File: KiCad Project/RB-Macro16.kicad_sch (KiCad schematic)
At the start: 67 parts, among them J1 USB_C_Receptacle, J2 AVR-ISP-6, K0A1 KEYSW, K0B1 KEYSW, K0C1 KEYSW, K0D1 KEYSW, K1A1 KEYSW, K1B1 KEYSW, K1C1 KEYSW, K1D1 KEYSW, K2A1 KEYSW, K2B1 KEYSW, K2C1 KEYSW, K2D1 KEYSW, K3A1 KEYSW, K3B1 KEYSW, K3C1 KEYSW, K3D1 KEYSW, SW1 SW_PUSH, U1 ATMEGA32U4, U2 CherryMX_LTST-A683CEGBW, X1 XTAL_GND

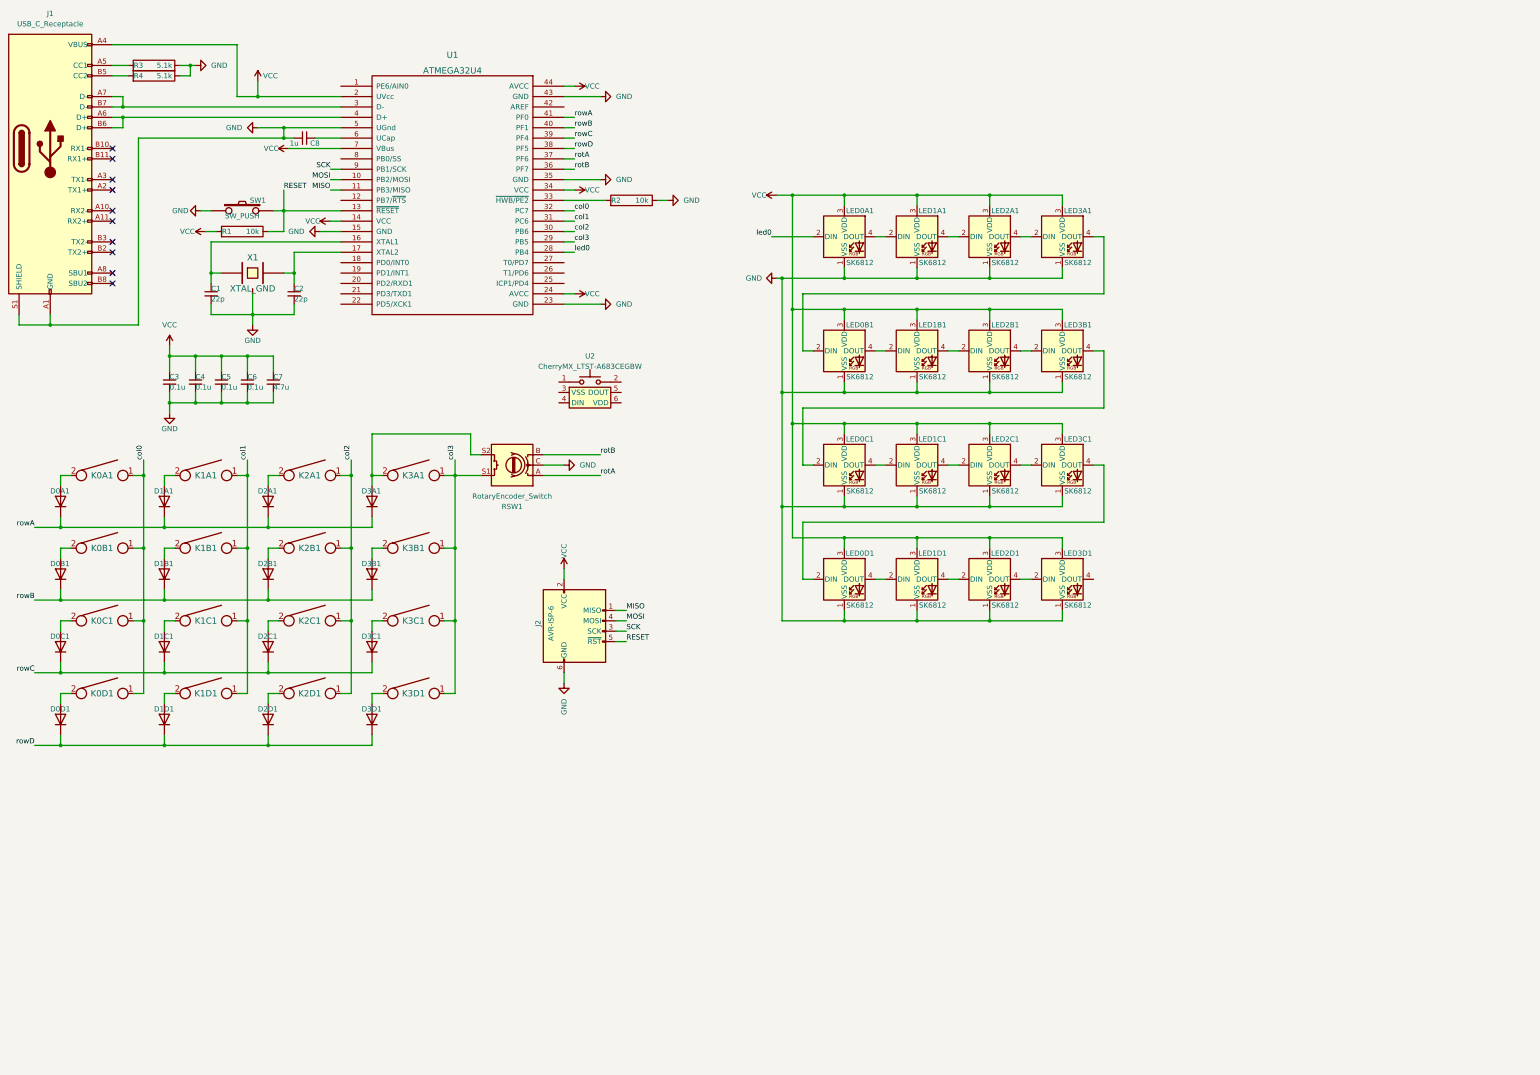
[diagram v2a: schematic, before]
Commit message: Abandoned New Swtich
Can't find LED new switch footprint uses. Began working on footprint for SK6812MINI-E from Adafruit as a replacement. Added capacitors to LED array and rebuilt it.
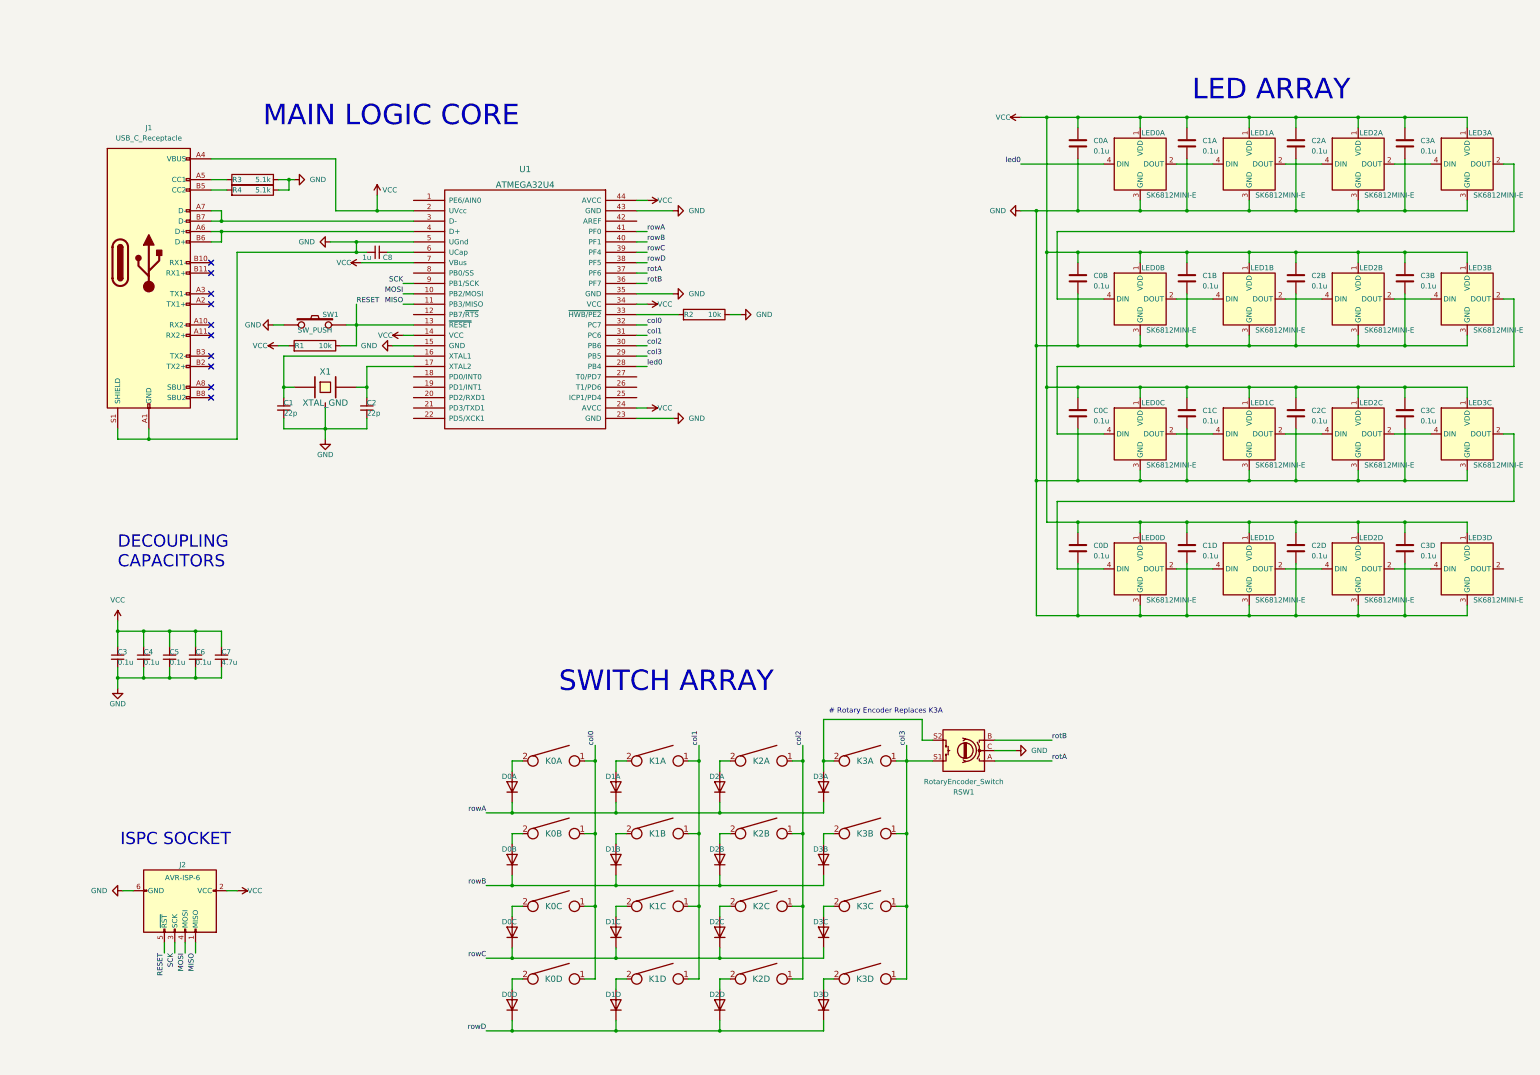
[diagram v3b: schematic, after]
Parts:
- removed LED0A1, LED0B1, LED0C1, LED0D1, LED1A1, LED1B1, LED1C1, LED1D1, LED2A1, LED2B1, LED2C1, LED2D1, LED3A1, LED3B1, LED3C1, LED3D1: SK6812, LED_SMD:LED_SK6812_EC15_1.5x1.5mm, symbol LED:SK6812
- removed U2: CherryMX_LTST-A683CEGBW, CherryMX_KailhSocket_LTST-A683CEGBW:CherryMX_1.00u_KailhSocket_LTST-A683CEGBW, symbol CherryMX:CherryMX_LTST-A683CEGBW
- added C0A, C0B, C0C, C0D, C1A, C1B, C1C, C1D, C2A, C2B, C2C, C2D, C3A, C3B, C3C, C3D: 0.1u, symbol Device:C
- added LED0A, LED0B, LED0C, LED0D, LED1A, LED1B, LED1C, LED1D, LED2A, LED2B, LED2C, LED2D, LED3A, LED3B, LED3C, LED3D: SK6812MINI-E, symbol RB_KeyboardParts:SK6812MINI-E
- J2: footprint keyboard_parts:AVR_ICSP_3x2 -> keyboard_parts.pretty-master:AVR_ICSP_3x2
- K0A: renamed from K0A1; footprint CherryMX_KailhSocket_LED:CherryMX_1.00u_KailhSocket_LED -> keyswitches.pretty-master:Kailh_socket_MX
- K0B: renamed from K0B1; footprint CherryMX_KailhSocket_LED:CherryMX_1.00u_KailhSocket_LED -> keyswitches.pretty-master:Kailh_socket_MX
- K0C: renamed from K0C1; footprint CherryMX_KailhSocket_LED:CherryMX_1.00u_KailhSocket_LED -> keyswitches.pretty-master:Kailh_socket_MX
- K0D: renamed from K0D1; footprint CherryMX_KailhSocket_LED:CherryMX_1.00u_KailhSocket_LED -> keyswitches.pretty-master:Kailh_socket_MX
- K1A: renamed from K1A1; footprint CherryMX_KailhSocket_LED:CherryMX_1.00u_KailhSocket_LED -> keyswitches.pretty-master:Kailh_socket_MX
- K1B: renamed from K1B1; footprint CherryMX_KailhSocket_LED:CherryMX_1.00u_KailhSocket_LED -> keyswitches.pretty-master:Kailh_socket_MX
- K1C: renamed from K1C1; footprint CherryMX_KailhSocket_LED:CherryMX_1.00u_KailhSocket_LED -> keyswitches.pretty-master:Kailh_socket_MX
- K1D: renamed from K1D1; footprint CherryMX_KailhSocket_LED:CherryMX_1.00u_KailhSocket_LED -> keyswitches.pretty-master:Kailh_socket_MX
- K2A: renamed from K2A1; footprint CherryMX_KailhSocket_LED:CherryMX_1.00u_KailhSocket_LED -> keyswitches.pretty-master:Kailh_socket_MX
- K2B: renamed from K2B1; footprint CherryMX_KailhSocket_LED:CherryMX_1.00u_KailhSocket_LED -> keyswitches.pretty-master:Kailh_socket_MX
- K2C: renamed from K2C1; footprint CherryMX_KailhSocket_LED:CherryMX_1.00u_KailhSocket_LED -> keyswitches.pretty-master:Kailh_socket_MX
- K2D: renamed from K2D1; footprint CherryMX_KailhSocket_LED:CherryMX_1.00u_KailhSocket_LED -> keyswitches.pretty-master:Kailh_socket_MX
- K3A: renamed from K3A1; footprint CherryMX_KailhSocket_LED:CherryMX_1.00u_KailhSocket_LED -> keyswitches.pretty-master:Kailh_socket_MX
- K3B: renamed from K3B1; footprint CherryMX_KailhSocket_LED:CherryMX_1.00u_KailhSocket_LED -> keyswitches.pretty-master:Kailh_socket_MX
- K3C: renamed from K3C1; footprint CherryMX_KailhSocket_LED:CherryMX_1.00u_KailhSocket_LED -> keyswitches.pretty-master:Kailh_socket_MX
- K3D: renamed from K3D1; footprint CherryMX_KailhSocket_LED:CherryMX_1.00u_KailhSocket_LED -> keyswitches.pretty-master:Kailh_socket_MX
- renumbered D0A1 to D0A, D0B1 to D0B, D0C1 to D0C, D0D1 to D0D, D1A1 to D1A, D1B1 to D1B, D1C1 to D1C, D1D1 to D1D, D2A1 to D2A, D2B1 to D2B, D2C1 to D2C, D2D1 to D2D, D3A1 to D3A, D3B1 to D3B, D3C1 to D3C, D3D1 to D3D
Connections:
- net GND: now also C0A.2, C0B.2, C0C.2, C0D.2, C1A.2, C1B.2, C1C.2, C1D.2, C2A.2, C2B.2, C2C.2, C2D.2, C3A.2, C3B.2, C3C.2, C3D.2, LED0A.3 (GND), LED0B.3 (GND), LED0C.3 (GND), LED0D.3 (GND), LED1A.3 (GND), LED1B.3 (GND), LED1C.3 (GND), LED1D.3 (GND), LED2A.3 (GND), LED2B.3 (GND), LED2C.3 (GND), LED2D.3 (GND), LED3A.3 (GND), LED3B.3 (GND), LED3C.3 (GND), LED3D.3 (GND)
- net VCC: now also C0A.1, C0B.1, C0C.1, C0D.1, C1A.1, C1B.1, C1C.1, C1D.1, C2A.1, C2B.1, C2C.1, C2D.1, C3A.1, C3B.1, C3C.1, C3D.1, LED0A.1 (VDD), LED0B.1 (VDD), LED0C.1 (VDD), LED0D.1 (VDD), LED1A.1 (VDD), LED1B.1 (VDD), LED1C.1 (VDD), LED1D.1 (VDD), LED2A.1 (VDD), LED2B.1 (VDD), LED2C.1 (VDD), LED2D.1 (VDD), LED3A.1 (VDD), LED3B.1 (VDD), LED3C.1 (VDD), LED3D.1 (VDD)
- net led0: now also LED0A.4 (DIN)
- new net: LED0B.2 (DOUT), LED1B.4 (DIN)
- new net: LED0B.4 (DIN), LED3A.2 (DOUT)
- new net: LED0C.2 (DOUT), LED1C.4 (DIN)
- new net: LED0C.4 (DIN), LED3B.2 (DOUT)
- new net: LED1B.2 (DOUT), LED2B.4 (DIN)
- new net: LED1A.2 (DOUT), LED2A.4 (DIN)
- new net: LED0A.2 (DOUT), LED1A.4 (DIN)
- new net: LED2D.2 (DOUT), LED3D.4 (DIN)
- new net: LED1D.2 (DOUT), LED2D.4 (DIN)
- new net: LED2A.2 (DOUT), LED3A.4 (DIN)
- new net: LED0D.4 (DIN), LED3C.2 (DOUT)
- new net: LED2C.2 (DOUT), LED3C.4 (DIN)
- new net: LED0D.2 (DOUT), LED1D.4 (DIN)
- new net: LED2B.2 (DOUT), LED3B.4 (DIN)
- new net: LED1C.2 (DOUT), LED2C.4 (DIN)
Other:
- note added: "# Rotary Encoder Replaces K3A"
- note added: "DECOUPLING CAPACITORS"
- note added: "ISPC SOCKET"
- note added: "LED ARRAY"
- note added: "MAIN LOGIC CORE"
- note added: "SWITCH ARRAY"
- moved on the sheet: C1, C2, C3, C4, C5, C6, C7, C8, D0A, D0B, D0C, D0D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

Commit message: New Switch Symbol and Footprint
Redid switch symbol and footprint to combine hot swap footprint and reverse mount LED footprint. Started work on PCB, laying out switches, diodes, capacitors
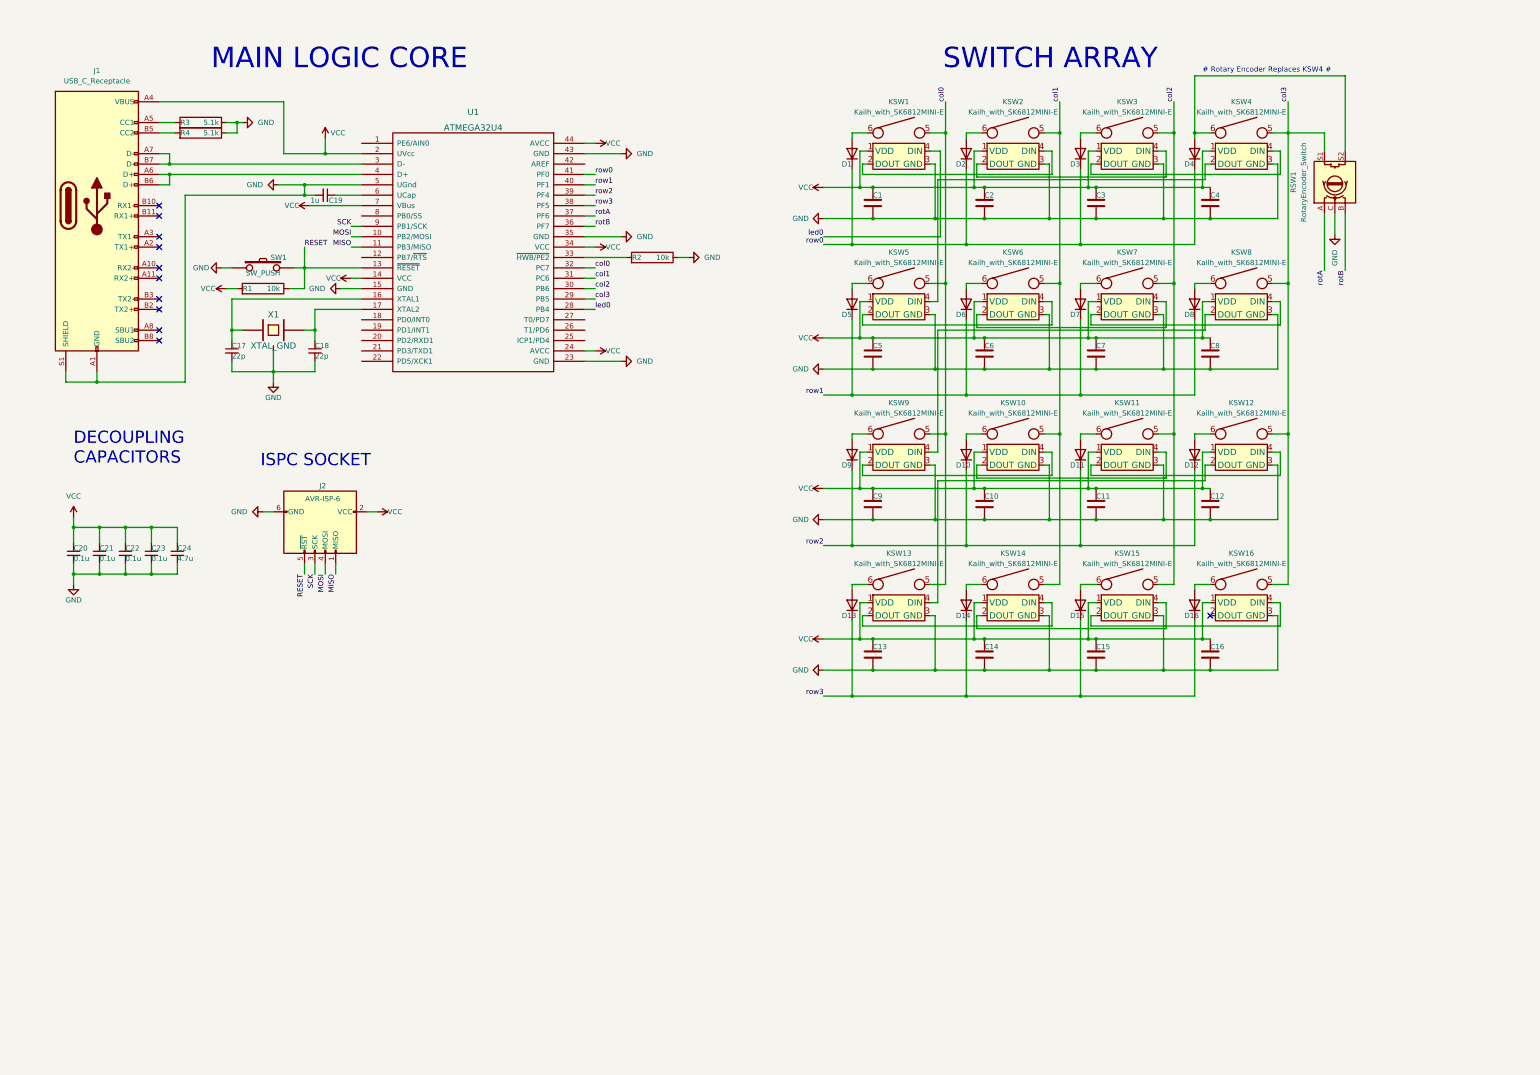
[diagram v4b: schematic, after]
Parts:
- removed C0A, C0B, C0C, C0D, C1A, C1B, C1C, C1D, C2A, C2B, C2C, C2D, C3A, C3B, C3C, C3D: 0.1u, symbol Device:C
- removed D0A, D0B, D0C, D0D, D1A, D1B, D1C, D1D, D2A, D2B, D2C, D2D, D3A, D3B, D3C, D3D: D, Diode_THT:D_DO-35_SOD27_P7.62mm_Horizontal, symbol Device:D
- removed K0A, K0B, K0C, K0D, K1A, K1B, K1C, K1D, K2A, K2B, K2C, K2D, K3A, K3B, K3C, K3D: KEYSW, keyswitches.pretty-master:Kailh_socket_MX, symbol keyboard_parts:KEYSW
- removed LED0A, LED0B, LED0C, LED0D, LED1A, LED1B, LED1C, LED1D, LED2A, LED2B, LED2C, LED2D, LED3A, LED3B, LED3C, LED3D: SK6812MINI-E, symbol RB_KeyboardParts:SK6812MINI-E
- added C1, C10, C11, C12, C13, C14, C15, C16, C2, C3, C4, C5, C6, C7, C8, C9: C, Capacitor_SMD:C_0805_2012Metric_Pad1.18x1.45mm_HandSolder, symbol Device:C
- added D1, D10, D11, D12, D13, D14, D15, D16, D2, D3, D4, D5, D6, D7, D8, D9: D, Diode_SMD:D_SOD-123, symbol Device:D
- added KSW1, KSW10, KSW11, KSW12, KSW13, KSW14, KSW15, KSW16, KSW2, KSW3, KSW4, KSW5, KSW6, KSW7, KSW8, KSW9: Kailh_with_SK6812MINI-E, RB_KeyboardParts:Kailh_with_SK6812MINI-E, symbol RB_KeyboardParts:Kailh_with_SK6812MINI-E
- RSW1: footprint Rotary_Encoder:RotaryEncoder_Alps_EC12E_Vertical_H20mm -> Rotary_Encoder:RotaryEncoder_Alps_EC12E-Switch_Vertical_H20mm
- renumbered C1 to C17, C2 to C18, C8 to C19, C3 to C20, C4 to C21, C5 to C22, C6 to C23, C7 to C24
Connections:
- net GND: now also C1.2, C10.2, C11.2, C12.2, C13.2, C14.2, C15.2, C16.2, C2.2, C3.2, C4.2, C5.2, C6.2, C7.2, C8.2, C9.2, KSW1.3 (GND), KSW10.3 (GND), KSW11.3 (GND), KSW12.3 (GND), KSW13.3 (GND), KSW14.3 (GND), KSW15.3 (GND), KSW16.3 (GND), KSW2.3 (GND), KSW3.3 (GND), KSW4.3 (GND), KSW5.3 (GND), KSW6.3 (GND), KSW7.3 (GND), KSW8.3 (GND), KSW9.3 (GND)
- net VCC: now also C1.1, C10.1, C11.1, C12.1, C13.1, C14.1, C15.1, C16.1, C2.1, C3.1, C4.1, C5.1, C6.1, C7.1, C8.1, C9.1, KSW1.1 (VDD), KSW10.1 (VDD), KSW11.1 (VDD), KSW12.1 (VDD), KSW13.1 (VDD), KSW14.1 (VDD), KSW15.1 (VDD), KSW16.1 (VDD), KSW2.1 (VDD), KSW3.1 (VDD), KSW4.1 (VDD), KSW5.1 (VDD), KSW6.1 (VDD), KSW7.1 (VDD), KSW8.1 (VDD), KSW9.1 (VDD)
- net col0: now also KSW1.5, KSW13.5, KSW5.5, KSW9.5
- net col1: now also KSW10.5, KSW14.5, KSW2.5, KSW6.5
- net col2: now also KSW11.5, KSW15.5, KSW3.5, KSW7.5
- net col3: now also KSW12.5, KSW16.5, KSW4.5, KSW8.5
- net led0: now also KSW1.4 (DIN)
- net at RSW1.S2: now also D4.2 (A), KSW4.6
- net rowA renamed row0
- net row0: now also D1.1 (K), D2.1 (K), D3.1 (K), D4.1 (K)
- net rowB renamed row1
- net row1: now also D5.1 (K), D6.1 (K), D7.1 (K), D8.1 (K)
- net rowC renamed row2
- net row2: now also D10.1 (K), D11.1 (K), D12.1 (K), D9.1 (K)
- net rowD renamed row3
- net row3: now also D13.1 (K), D14.1 (K), D15.1 (K), D16.1 (K)
- new net: D1.2 (A), KSW1.6
- new net: KSW4.2 (DOUT), KSW5.4 (DIN)
- new net: KSW3.2 (DOUT), KSW4.4 (DIN)
- new net: KSW8.2 (DOUT), KSW9.4 (DIN)
- new net: KSW7.2 (DOUT), KSW8.4 (DIN)
- new net: D8.2 (A), KSW8.6
- new net: D9.2 (A), KSW9.6
- new net: D7.2 (A), KSW7.6
- new net: D11.2 (A), KSW11.6
- new net: KSW15.2 (DOUT), KSW16.4 (DIN)
- new net: KSW14.2 (DOUT), KSW15.4 (DIN)
- new net: D15.2 (A), KSW15.6
- new net: KSW10.2 (DOUT), KSW11.4 (DIN)
- new net: KSW10.4 (DIN), KSW9.2 (DOUT)
- new net: D10.2 (A), KSW10.6
- new net: D5.2 (A), KSW5.6
- new net: KSW6.2 (DOUT), KSW7.4 (DIN)
- new net: KSW5.2 (DOUT), KSW6.4 (DIN)
- new net: D6.2 (A), KSW6.6
- new net: KSW2.2 (DOUT), KSW3.4 (DIN)
- new net: KSW1.2 (DOUT), KSW2.4 (DIN)
- new net: D2.2 (A), KSW2.6
- new net: D16.2 (A), KSW16.6
- new net: KSW13.2 (DOUT), KSW14.4 (DIN)
- new net: D14.2 (A), KSW14.6
- new net: KSW12.2 (DOUT), KSW13.4 (DIN)
- new net: KSW11.2 (DOUT), KSW12.4 (DIN)
- new net: D12.2 (A), KSW12.6
- new net: D13.2 (A), KSW13.6
- new net: D3.2 (A), KSW3.6
- no-connect marks 10 -> 11
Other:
- note added: "# Rotary Encoder Replaces KSW4 #"
- note removed: "# Rotary Encoder Replaces K3A"
- note removed: "LED ARRAY"
- moved on the sheet: C17, C18, C19, C20, C21, C22, C23, C24, J1, J2, R1, R2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

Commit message: Routed PCB
Routed most of the traces in the PCB for the switch block. uP in progress.
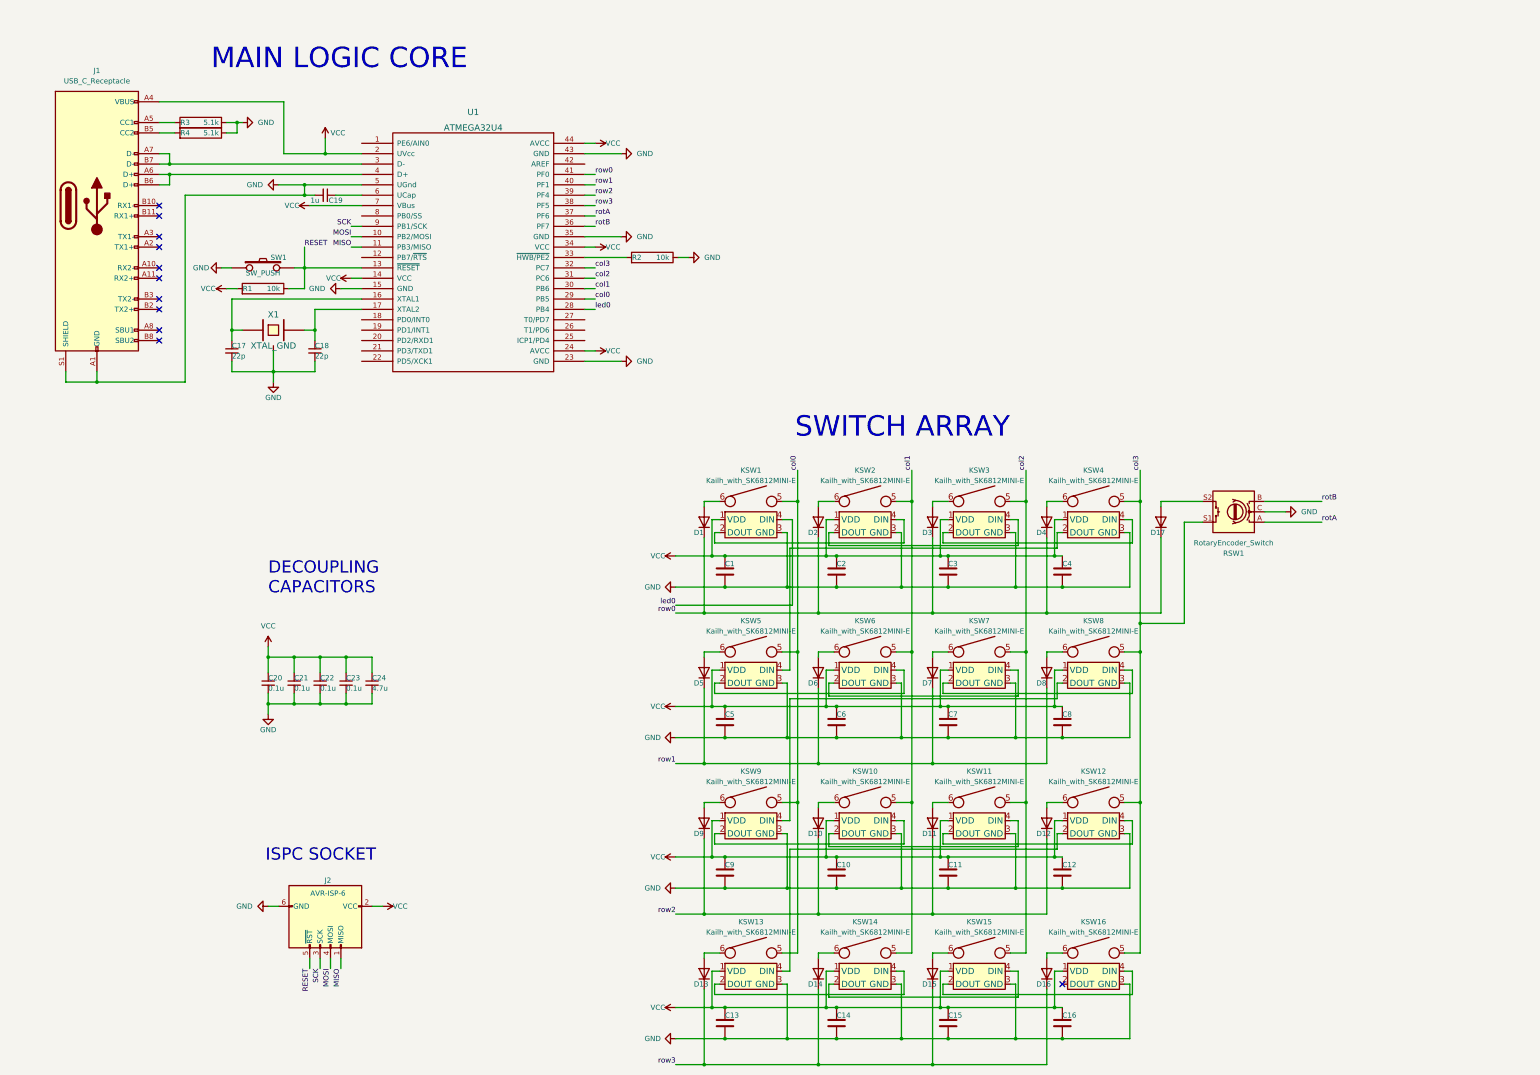
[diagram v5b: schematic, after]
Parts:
- added D17: D, Diode_SMD:D_SOD-123, symbol Device:D
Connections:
- net col0: now also U1.29 (PB5); no longer U1.32 (PC7)
- net col1: now also U1.30 (PB6); no longer U1.31 (PC6)
- net col2: now also U1.31 (PC6); no longer U1.30 (PB6)
- net col3: now also U1.32 (PC7); no longer U1.29 (PB5)
- net row0: now also D17.1 (K)
- net at D4.2 (A), KSW4.6: no longer RSW1.S2
- new net: D17.2 (A), RSW1.S2
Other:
- note removed: "# Rotary Encoder Replaces KSW4 #"
- moved on the sheet: C1, C10, C11, C12, C13, C14, C15, C16, C2, C20, C21, C22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

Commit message: Generated BOM
BOM
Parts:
- C1, C10, C11, C12, C13, C14, C15, C16, C2, C3, C4, C5, C6, C7, C8, C9: value C -> 0.1u
